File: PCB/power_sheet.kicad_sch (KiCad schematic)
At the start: 1 part, among them U2 BQ24072RGT

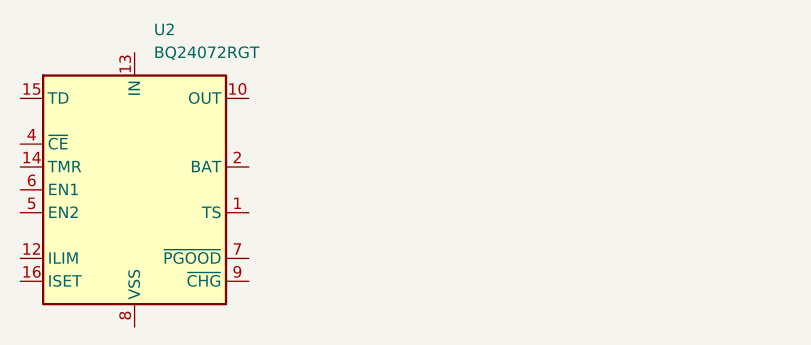
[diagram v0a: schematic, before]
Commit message: realized the magnetic sensor wont work because of orientation
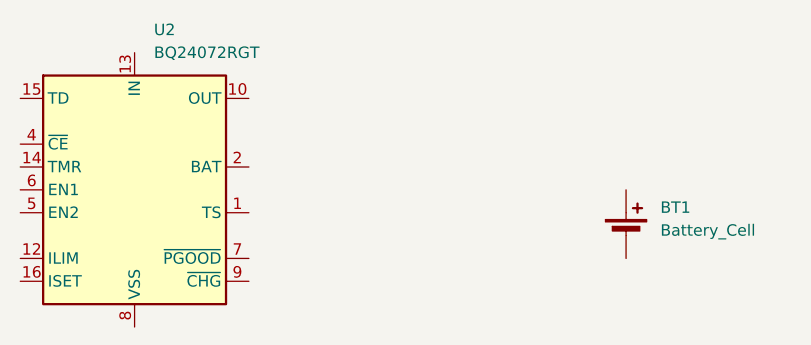
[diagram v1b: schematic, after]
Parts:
- added BT1: Battery_Cell, symbol Device:Battery_Cell
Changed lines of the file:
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@@
+		)
+	)
+	(symbol
+		(lib_id "Device:Battery_Cell")
+		(at 207.01 102.87 0)
+		(unit 1)
+		(exclude_from_sim no)
+		(in_bom yes)
+		(on_board yes)
+		(dnp no)
+		(fields_autoplaced yes)
+		(property "Reference" "BT1"
+			(at 210.82 99.7584 0)
+			(effects
+				(font
+					(size 1.27 1.27)
+				)
+				(justify left)
+			)
+		)
+		(property "Value" "Battery_Cell"
+			(at 210.82 102.2984 0)
+			(effects
+				(font
+					(size 1.27 1.27)
+				)
+				(justify left)
+			)
+		)
+		(property "Footprint" ""
+			(at 207.01 101.346 90)
+			(effects
+				(font
+					(size 1.27 1.27)
+				)
+				(hide yes)
+			)
+		)
+		(property "Datasheet" "~"
+			(at 207.01 101.346 90)
+			(effects
+				(font
+					(size 1.27 1.27)
+				)
+				(hide yes)
+			)
+		)
+		(property "Description" "Single-cell battery"
+			(at 207.01 102.87 0)
+			(effects
+				(font
+					(size 1.27 1.27)
+				)
+				(hide yes)
+			)
+		)
+		(property "Sim.Device" "V"
+			(at 207.01 102.87 0)
+			(effects
+				(font
+					(size 1.27 1.27)
+				)
+				(hide yes)
+			)
+		)
+		(property "Sim.Type" "DC"
+			(at 207.01 102.87 0)
+			(effects
+				(font
+					(size 1.27 1.27)
+				)
+				(hide yes)
+			)
+		)
+		(property "Sim.Pins" "1=+ 2=-"
+			(at 207.01 102.87 0)
+			(effects
+				(font
+					(size 1.27 1.27)
+				)
+				(hide yes)
+			)
+		)
+		(pin "1"
+		)
+		(pin "2"
+		)
+		(instances
+			(project ""
+				(path "/676a96c8-df44-4067-be01-152bfa3def97/84cf4740-f9fd-4d53-b02f-66827250f642"
+					(reference "BT1")
+					(unit 1)
+				)
+			)
 		)
 	)
